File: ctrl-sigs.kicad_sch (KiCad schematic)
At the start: 11 parts, among them U5 LTV-817S, U6 TLP184

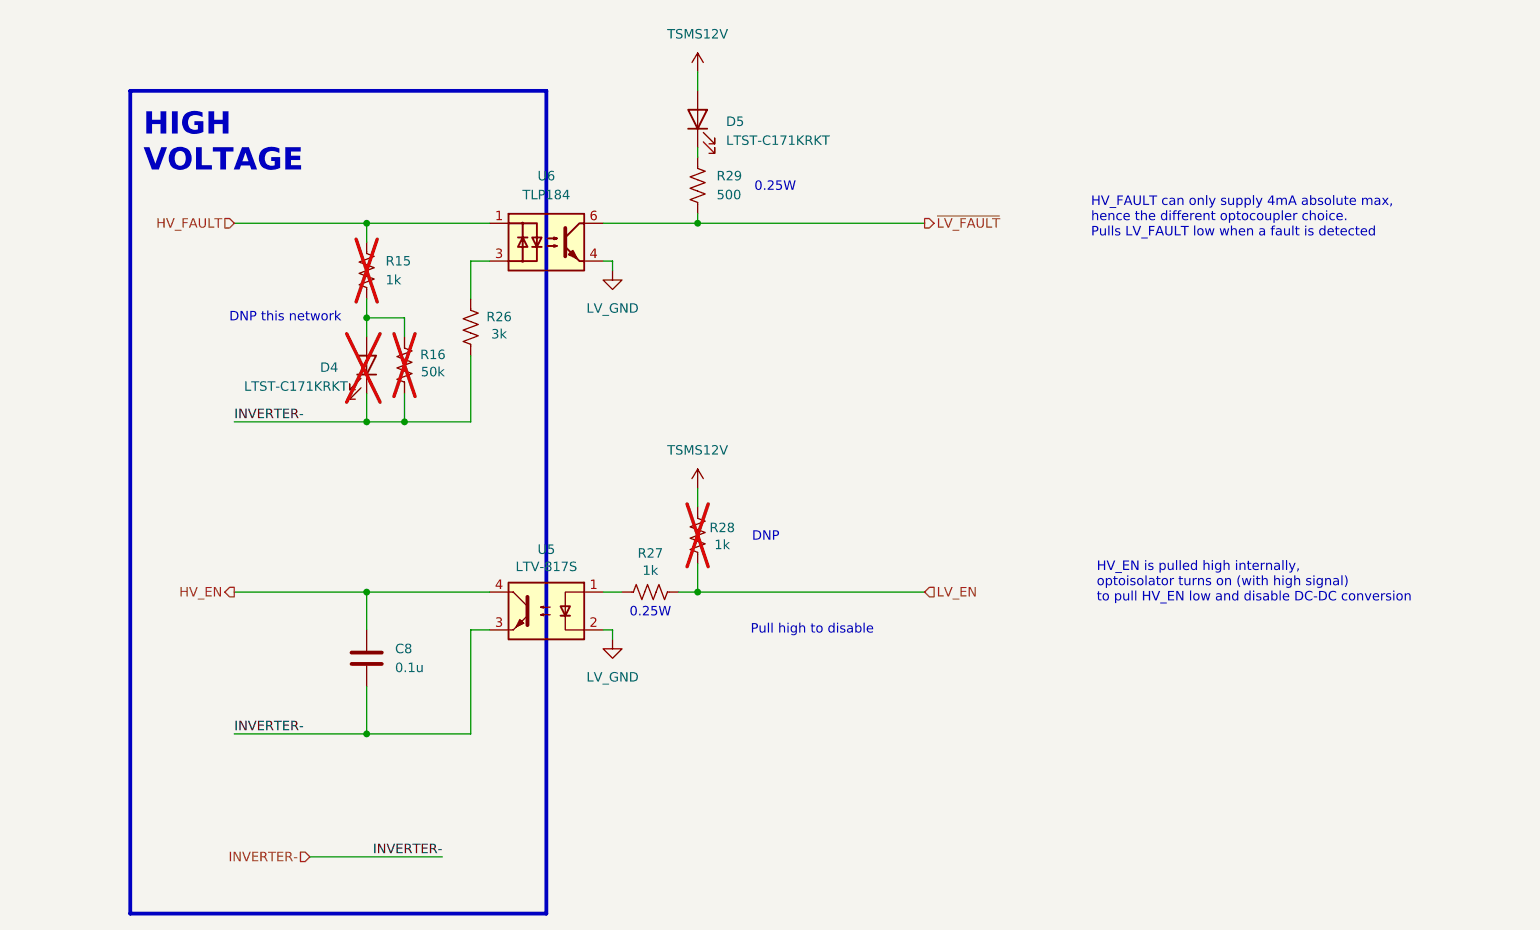
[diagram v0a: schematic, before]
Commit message: Started layout
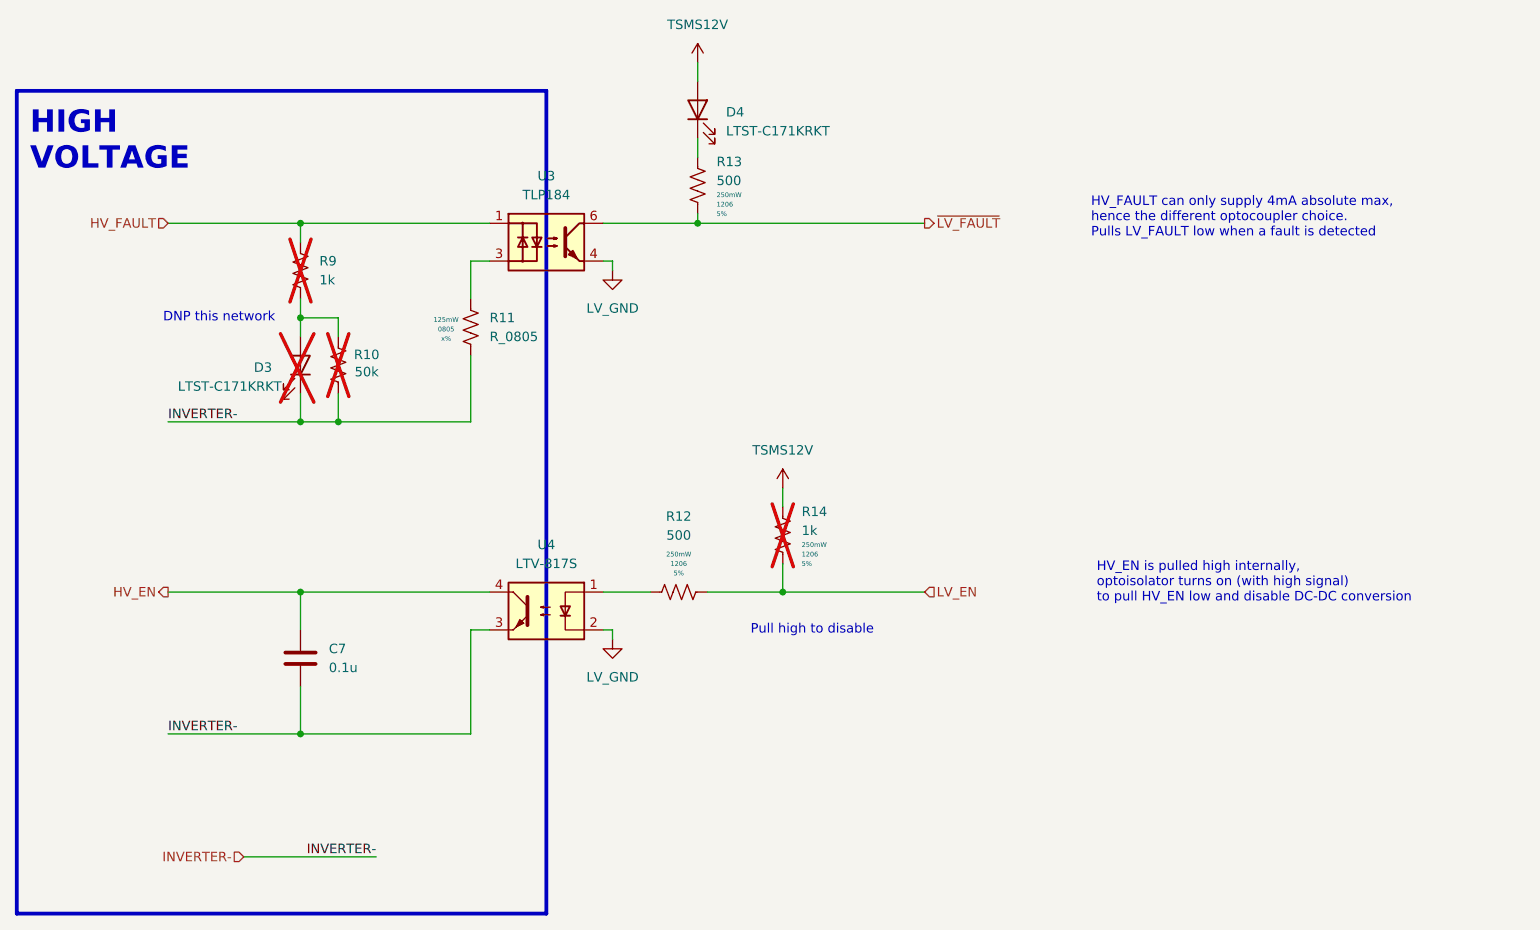
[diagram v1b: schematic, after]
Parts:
- removed R26: 3k, Resistor_SMD:R_0603_1608Metric_Pad0.98x0.95mm_HandSolder, symbol Device:R_US
- removed R27: 1k, Resistor_SMD:R_0805_2012Metric_Pad1.20x1.40mm_HandSolder, symbol Device:R_US
- removed R28: 1k, Resistor_SMD:R_0603_1608Metric_Pad0.98x0.95mm_HandSolder, symbol Device:R_US
- removed R29: 500, Resistor_SMD:R_0805_2012Metric_Pad1.20x1.40mm_HandSolder, symbol Device:R_US
- removed U5: LTV-817S, Package_DIP:SMDIP-4_W9.53mm, symbol Isolator:LTV-817S
- added R11: R_0805, Resistor_SMD:R_0805_2012Metric_Pad1.20x1.40mm_HandSolder, symbol AERO_Resistors:R_0805
- added R12, R13: 500, Resistor_SMD:R_1206_3216Metric_Pad1.30x1.75mm_HandSolder, symbol AERO_Resistors:R_1206
- added R14: 1k, Resistor_SMD:R_1206_3216Metric_Pad1.30x1.75mm_HandSolder, symbol AERO_Resistors:R_1206
- added U4: LTV-817S, Package_DIP:SMDIP-4_W9.53mm, symbol Isolator:LTV-817S
- renumbered C8 to C7, D4 to D3, D5 to D4, R16 to R10, R15 to R9, U6 to U3
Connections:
- net HV_EN: now also U4.4
- net INVERTER-: now also R11.2, U4.3
- net LV_EN: now also R12.2, R14.1
- net LV_GND: now also U4.2
- net TSMS12V: now also R14.2
- net ~{LV_FAULT}: now also R13.1
- net at D4.1 (K): now also R13.2
- net at U3.3: now also R11.1
- new net: R12.1, U4.1
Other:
- note removed: "0.25W"
- note removed: "DNP"
- moved on the sheet: C7, D3, D4, R10, R9
